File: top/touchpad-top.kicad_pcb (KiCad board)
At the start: 4 copper layers, 28.3 x 40 mm, 18 parts, among them P1 CONN_10, P2 CONN_5, U1 IQS572, U4 ESD

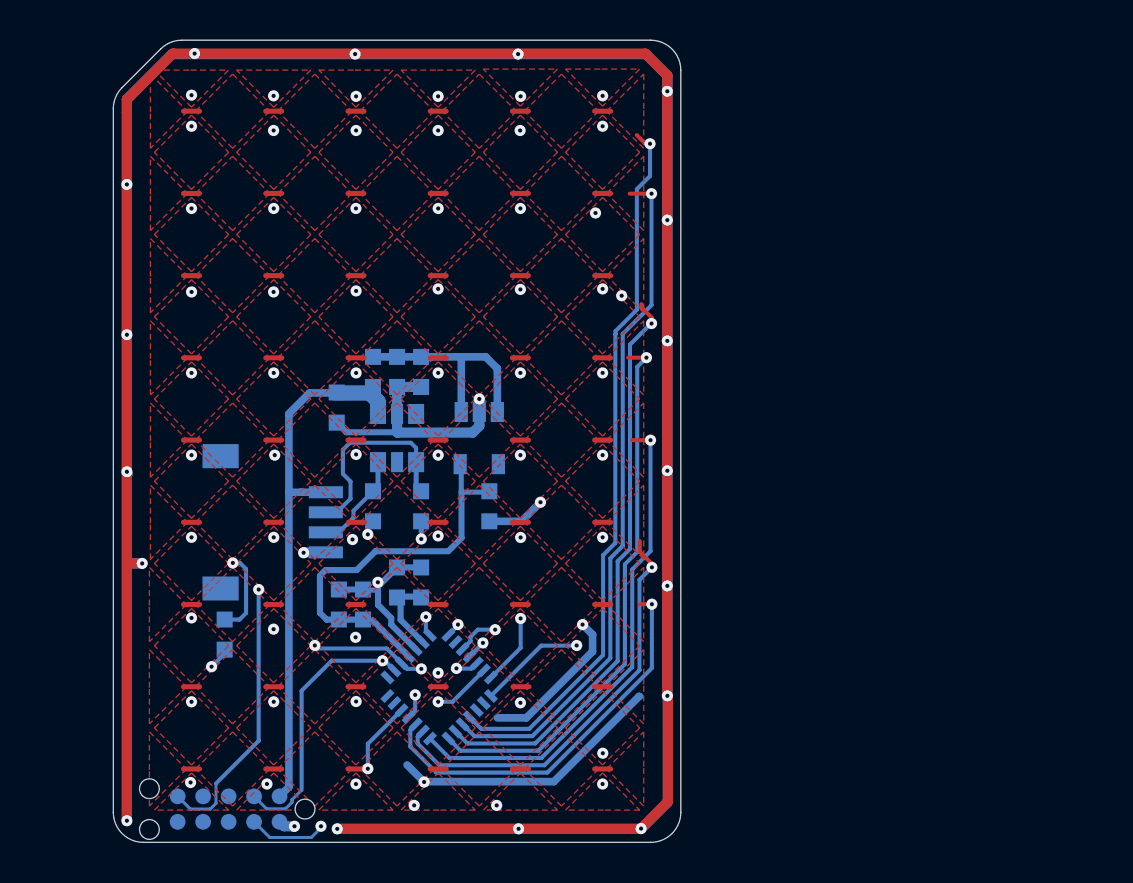
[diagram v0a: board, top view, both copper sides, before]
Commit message: Add GND island into capacitive pads.
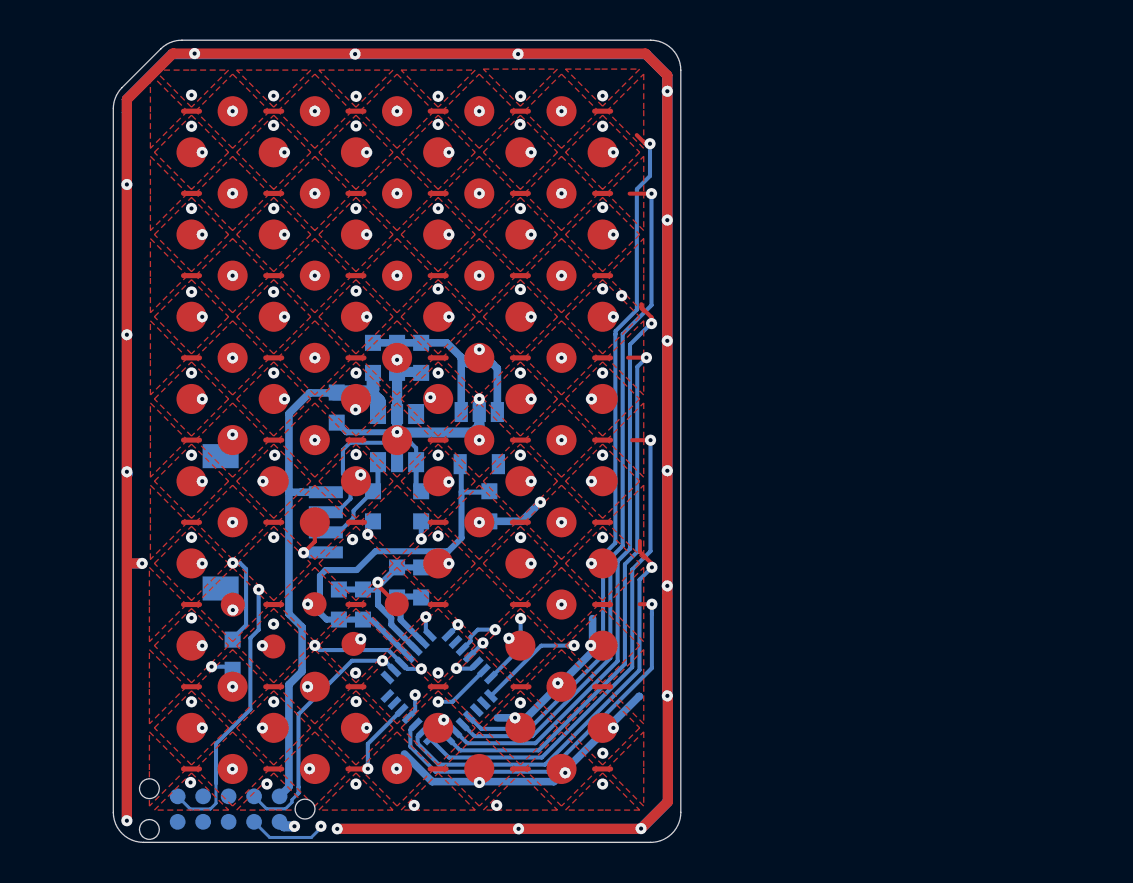
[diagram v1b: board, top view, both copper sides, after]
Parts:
- added hole: 1.5mm, UGL:smd_pad_1.5mm, F.Cu at (209.8, 154.8)
- added hole: 1.5mm, UGL:smd_pad_1.5mm, F.Cu at (211.8, 148.7)
- added hole: 1.5mm, UGL:smd_pad_1.5mm, F.Cu at (195.4, 148.7)
- added hole: 1.5mm, UGL:smd_pad_1.5mm, F.Cu at (215.9, 144.6)
- added hole: 1.5mm, UGL:smd_pad_1.5mm, F.Cu at (211.8, 144.6)
- added hole: 1.5mm, UGL:smd_pad_1.5mm, F.Cu at (207.8, 144.6)
- added hole: 1.5mm, UGL:smd_pad_1.5mm, F.Cu at (195.4, 144.6)
- added hole: 1.5mm, UGL:smd_pad_1.5mm, F.Cu at (215.9, 140.4)
- added hole: 1.5mm, UGL:smd_pad_1.5mm, F.Cu at (211.8, 140.4)
- added hole: 1.5mm, UGL:smd_pad_1.5mm, F.Cu at (207.8, 140.4)
- added hole: 1.5mm, UGL:smd_pad_1.5mm, F.Cu at (203.7, 140.4)
- added hole: 1.5mm, UGL:smd_pad_1.5mm, F.Cu at (197.5, 142.5)
- added hole: 1.5mm, UGL:smd_pad_1.5mm, F.Cu at (199.6, 140.4)
- added hole: 1.5mm, UGL:smd_pad_1.5mm, F.Cu at (195.4, 140.4)
- added hole: 1.5mm, UGL:smd_pad_1.5mm, F.Cu at (215.9, 136.3)
- added hole: 1.5mm, UGL:smd_pad_1.5mm, F.Cu at (211.8, 136.3)
- added hole: 1.5mm, UGL:smd_pad_1.5mm, F.Cu at (207.8, 136.3)
- added hole: 1.5mm, UGL:smd_pad_1.5mm, F.Cu at (203.7, 136.3)
- added hole: 1.5mm, UGL:smd_pad_1.5mm, F.Cu at (199.6, 136.3)
- added hole: 1.5mm, UGL:smd_pad_1.5mm, F.Cu at (195.4, 136.3)
- added hole: 1.5mm, UGL:smd_pad_1.5mm, F.Cu at (215.9, 132.2)
- added hole: 1.5mm, UGL:smd_pad_1.5mm, F.Cu at (211.8, 132.2)
- added hole: 1.5mm, UGL:smd_pad_1.5mm, F.Cu at (215.9, 152.8)
- added hole: 1.5mm, UGL:smd_pad_1.5mm, F.Cu at (207.8, 132.2)
- added hole: 1.5mm, UGL:smd_pad_1.5mm, F.Cu at (203.7, 132.2)
- added hole: 1.5mm, UGL:smd_pad_1.5mm, F.Cu at (199.6, 132.2)
- added hole: 1.5mm, UGL:smd_pad_1.5mm, F.Cu at (195.4, 132.2)
- added hole: 1.5mm, UGL:smd_pad_1.5mm, F.Cu at (215.9, 128.2)
- added hole: 1.5mm, UGL:smd_pad_1.5mm, F.Cu at (211.8, 128.2)
- added hole: 1.5mm, UGL:smd_pad_1.5mm, F.Cu at (207.8, 128.2)
- added hole: 1.5mm, UGL:smd_pad_1.5mm, F.Cu at (203.7, 128.2)
- added hole: 1.5mm, UGL:smd_pad_1.5mm, F.Cu at (199.6, 128.2)
- added hole: 1.5mm, UGL:smd_pad_1.5mm, F.Cu at (195.4, 128.2)
- added hole: 1.5mm, UGL:smd_pad_1.5mm, F.Cu at (211.8, 152.8)
- added hole: 1.5mm, UGL:smd_pad_1.5mm, F.Cu at (215.9, 124.0)
- added hole: 1.5mm, UGL:smd_pad_1.5mm, F.Cu at (211.8, 124.0)
- added hole: 1.5mm, UGL:smd_pad_1.5mm, F.Cu at (207.8, 124.0)
- added hole: 1.5mm, UGL:smd_pad_1.5mm, F.Cu at (203.7, 124.0)
- added hole: 1.5mm, UGL:smd_pad_1.5mm, F.Cu at (199.6, 124.0)
- added hole: 1.5mm, UGL:smd_pad_1.5mm, F.Cu at (195.4, 124.0)
- added hole: 1.5mm, UGL:smd_pad_1.5mm, F.Cu at (213.9, 154.8)
- added hole: 1.5mm, UGL:smd_pad_1.5mm, F.Cu at (205.7, 154.8)
- added hole: 1.5mm, UGL:smd_pad_1.5mm, F.Cu at (201.6, 154.8)
- added hole: 1.5mm, UGL:smd_pad_1.5mm, F.Cu at (197.5, 154.8)
- added hole: 1.5mm, UGL:smd_pad_1.5mm, F.Cu at (207.8, 152.8)
- added hole: 1.5mm, UGL:smd_pad_1.5mm, F.Cu at (213.9, 150.7)
- added hole: 1.5mm, UGL:smd_pad_1.5mm, F.Cu at (201.6, 150.7)
- added hole: 1.5mm, UGL:smd_pad_1.5mm, F.Cu at (197.5, 150.7)
- added hole: 1.5mm, UGL:smd_pad_1.5mm, F.Cu at (213.9, 146.6)
- added hole: 1.5mm, UGL:smd_pad_1.5mm, F.Cu at (213.9, 142.5)
- added hole: 1.5mm, UGL:smd_pad_1.5mm, F.Cu at (209.8, 142.5)
- added hole: 1.5mm, UGL:smd_pad_1.5mm, F.Cu at (201.6, 142.5)
- added hole: 1.5mm, UGL:smd_pad_1.5mm, F.Cu at (213.9, 138.4)
- added hole: 1.5mm, UGL:smd_pad_1.5mm, F.Cu at (209.8, 138.4)
- added hole: 1.5mm, UGL:smd_pad_1.5mm, F.Cu at (205.7, 138.4)
- added hole: 1.5mm, UGL:smd_pad_1.5mm, F.Cu at (203.7, 152.8)
- added hole: 1.5mm, UGL:smd_pad_1.5mm, F.Cu at (201.6, 138.4)
- added hole: 1.5mm, UGL:smd_pad_1.5mm, F.Cu at (197.5, 138.4)
- added hole: 1.5mm, UGL:smd_pad_1.5mm, F.Cu at (213.9, 134.3)
- added hole: 1.5mm, UGL:smd_pad_1.5mm, F.Cu at (209.8, 134.3)
- added hole: 1.5mm, UGL:smd_pad_1.5mm, F.Cu at (205.7, 134.3)
- added hole: 1.5mm, UGL:smd_pad_1.5mm, F.Cu at (201.6, 134.3)
- added hole: 1.5mm, UGL:smd_pad_1.5mm, F.Cu at (197.5, 134.3)
- added hole: 1.5mm, UGL:smd_pad_1.5mm, F.Cu at (213.9, 130.2)
- added hole: 1.5mm, UGL:smd_pad_1.5mm, F.Cu at (209.8, 130.2)
- added hole: 1.5mm, UGL:smd_pad_1.5mm, F.Cu at (205.7, 130.2)
- added hole: 1.5mm, UGL:smd_pad_1.5mm, F.Cu at (199.6, 152.8)
- added hole: 1.5mm, UGL:smd_pad_1.5mm, F.Cu at (201.6, 130.2)
- added hole: 1.5mm, UGL:smd_pad_1.5mm, F.Cu at (197.5, 130.2)
- added hole: 1.5mm, UGL:smd_pad_1.5mm, F.Cu at (213.9, 126.1)
- added hole: 1.5mm, UGL:smd_pad_1.5mm, F.Cu at (209.8, 126.1)
- added hole: 1.5mm, UGL:smd_pad_1.5mm, F.Cu at (205.7, 126.1)
- added hole: 1.5mm, UGL:smd_pad_1.5mm, F.Cu at (201.6, 126.1)
- added hole: 1.5mm, UGL:smd_pad_1.5mm, F.Cu at (197.5, 126.1)
- added hole: 1.5mm, UGL:smd_pad_1.5mm, F.Cu at (213.9, 122.0)
- added hole: 1.5mm, UGL:smd_pad_1.5mm, F.Cu at (209.8, 122.0)
- added hole: 1.5mm, UGL:smd_pad_1.5mm, F.Cu at (205.7, 122.0)
- added hole: 1.5mm, UGL:smd_pad_1.5mm, F.Cu at (195.4, 152.8)
- added hole: 1.5mm, UGL:smd_pad_1.5mm, F.Cu at (201.6, 122.0)
- added hole: 1.5mm, UGL:smd_pad_1.5mm, F.Cu at (197.5, 122.0)
- added hole: 1.5mm, UGL:smd_pad_1.5mm, F.Cu at (215.9, 148.7)
- added pad: 1.2mm, UGL:smd_pad_1.2mm, F.Cu at (203.5, 148.6)
- added pad: 1.2mm, UGL:smd_pad_1.2mm, F.Cu at (197.5, 146.6)
- added pad: 1.2mm, UGL:smd_pad_1.2mm, F.Cu at (199.5, 148.7)
- added pad: 1.2mm, UGL:smd_pad_1.2mm, F.Cu at (205.7, 146.6)
- added pad: 1.2mm, UGL:smd_pad_1.2mm, F.Cu at (201.6, 146.6)
- moved C1 1.08 mm to (197.5, 149.1)
- moved C2 0.70 mm to (205.7, 134.3)
- moved C8 0.70 mm to (206.9, 134.3)
- moved FB2 0.70 mm to (204.5, 134.3)
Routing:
- net GND: track 471.4 -> 476.0 mm, vias 26 -> 108
- net /VCC_BOTTOM: track 26.8 -> 28.4 mm
- net /RX2: track 41.5 -> 42.6 mm
- net /SDA: track 21.1 -> 20.4 mm
- net /RX3: track 39.1 -> 39.7 mm

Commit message: Bump top board version to 2.3.0
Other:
- board text added: "PCB_ID: touchpad_top_2.3.0"
- board text removed: "PCB_ID: touchpad_top_2.2.0"

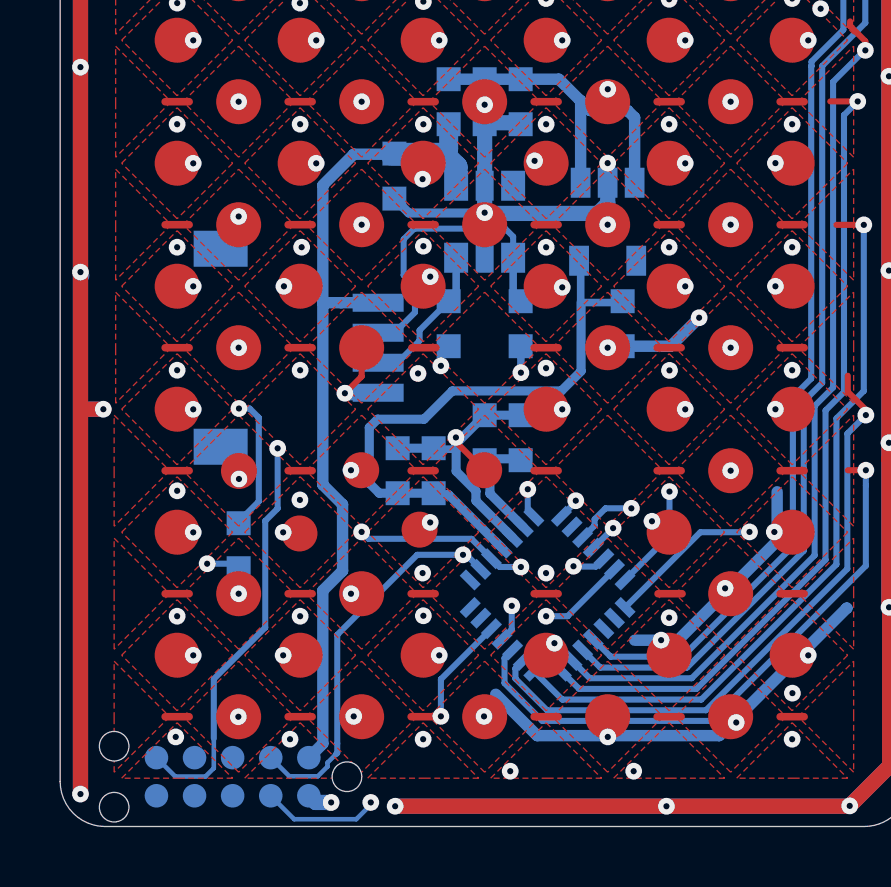
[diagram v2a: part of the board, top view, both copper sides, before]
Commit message: Modified SCL and SDA routing.
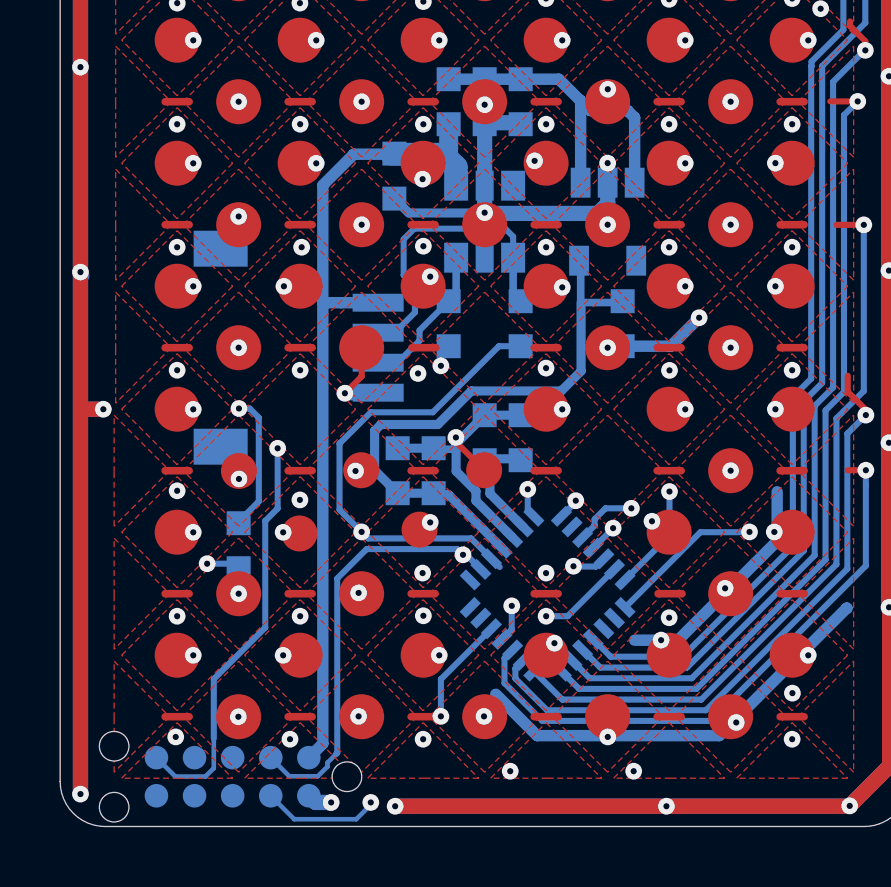
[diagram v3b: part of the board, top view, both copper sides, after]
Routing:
- net /SCL: track 26.6 -> 29.4 mm, vias 4 -> 2
- net /SDA: track 20.4 -> 21.7 mm
- net +3V3: track 19.4 -> 18.8 mm
- net /VCC_BOTTOM: track 28.4 -> 27.9 mm

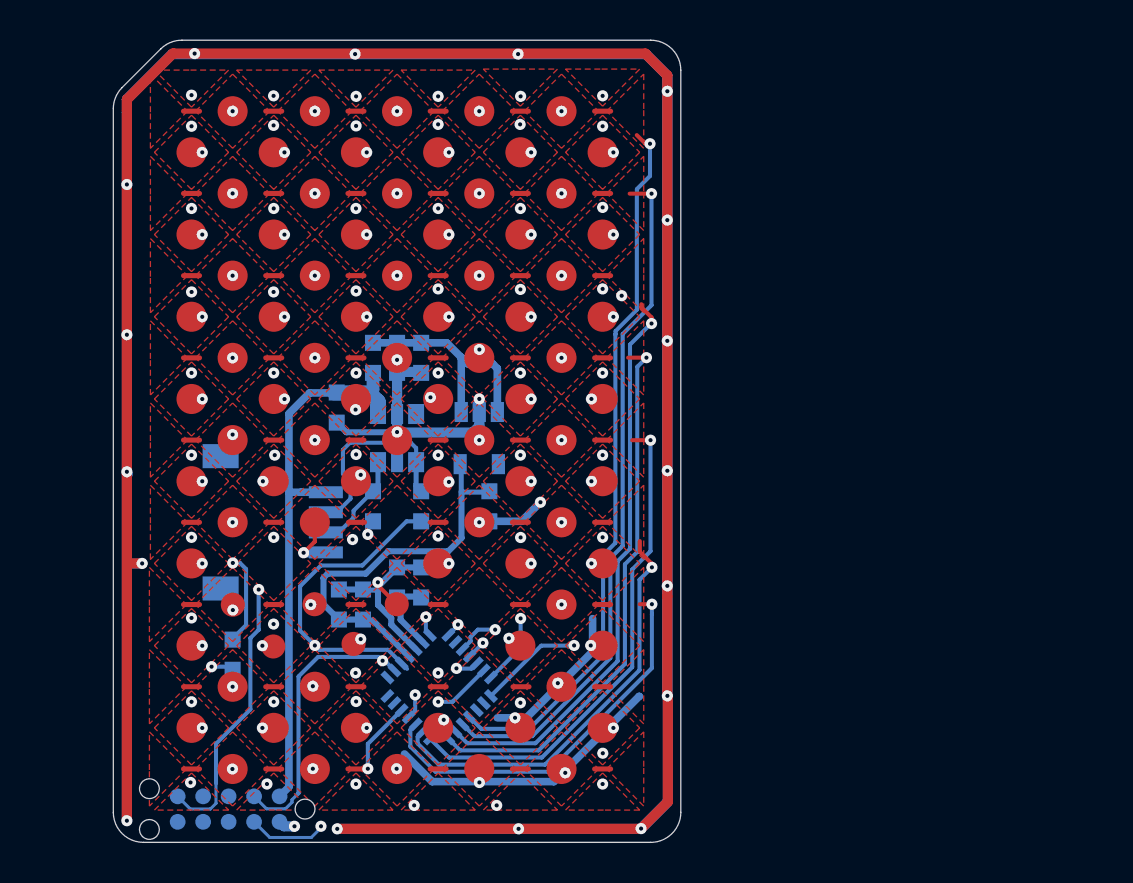
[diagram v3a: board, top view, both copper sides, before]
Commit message: Change board stackup and remove gnd islands.
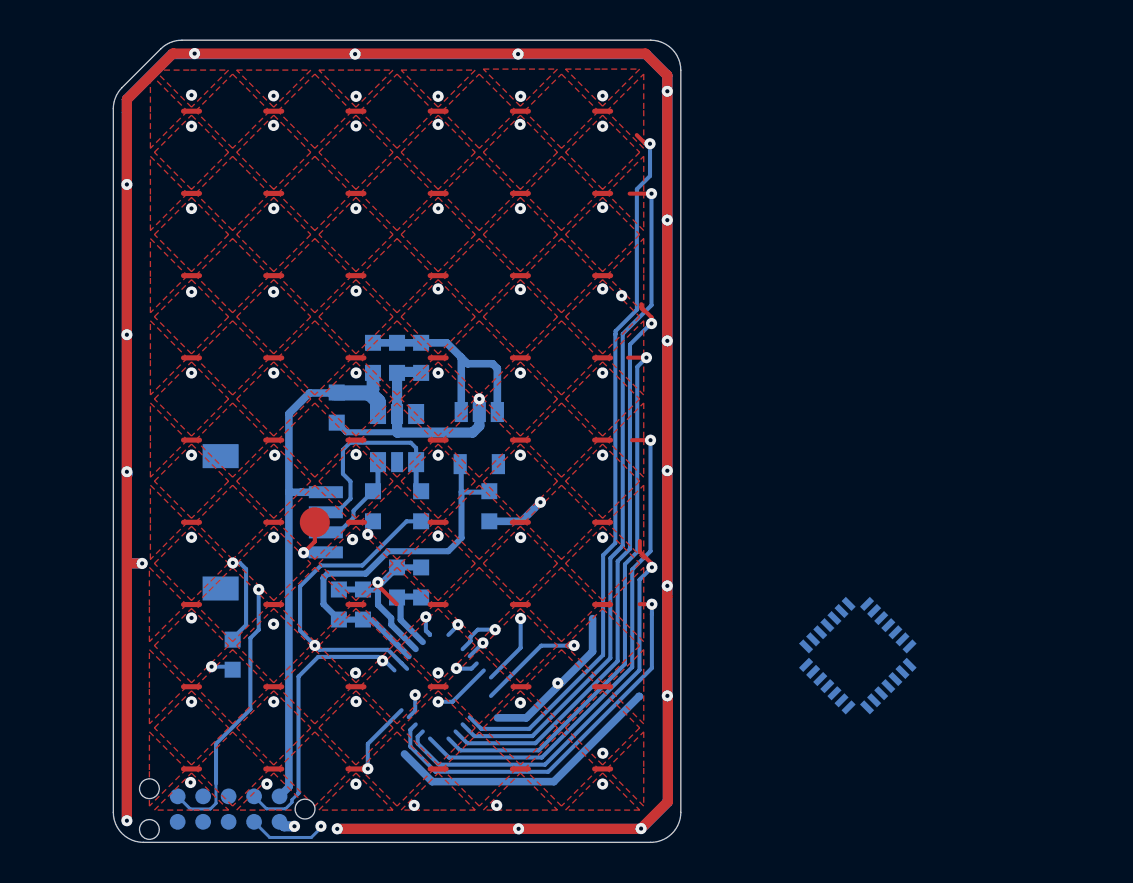
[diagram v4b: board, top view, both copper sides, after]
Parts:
- removed the hole at (209.8, 154.8)
- removed the hole at (211.8, 148.7)
- removed the hole at (195.4, 148.7)
- removed the hole at (215.9, 144.6)
- removed the hole at (211.8, 144.6)
- removed the hole at (207.8, 144.6)
- removed the hole at (195.4, 144.6)
- removed the hole at (215.9, 140.4)
- removed the hole at (211.8, 140.4)
- removed the hole at (207.8, 140.4)
- removed the hole at (203.7, 140.4)
- removed the hole at (197.5, 142.5)
- removed the hole at (199.6, 140.4)
- removed the hole at (195.4, 140.4)
- removed the hole at (215.9, 136.3)
- removed the hole at (211.8, 136.3)
- removed the hole at (207.8, 136.3)
- removed the hole at (203.7, 136.3)
- removed the hole at (199.6, 136.3)
- removed the hole at (195.4, 136.3)
- removed the hole at (215.9, 132.2)
- removed the hole at (211.8, 132.2)
- removed the hole at (215.9, 152.8)
- removed the hole at (207.8, 132.2)
- removed the hole at (203.7, 132.2)
- removed the hole at (199.6, 132.2)
- removed the hole at (195.4, 132.2)
- removed the hole at (215.9, 128.2)
- removed the hole at (211.8, 128.2)
- removed the hole at (207.8, 128.2)
- removed the hole at (203.7, 128.2)
- removed the hole at (199.6, 128.2)
- removed the hole at (195.4, 128.2)
- removed the hole at (211.8, 152.8)
- removed the hole at (215.9, 124.0)
- removed the hole at (211.8, 124.0)
- removed the hole at (207.8, 124.0)
- removed the hole at (203.7, 124.0)
- removed the hole at (199.6, 124.0)
- removed the hole at (195.4, 124.0)
- removed the hole at (213.9, 154.8)
- removed the hole at (205.7, 154.8)
- removed the hole at (201.6, 154.8)
- removed the hole at (197.5, 154.8)
- removed the hole at (207.8, 152.8)
- removed the hole at (213.9, 150.7)
- removed the hole at (201.6, 150.7)
- removed the hole at (197.5, 150.7)
- removed the hole at (213.9, 146.6)
- removed the hole at (213.9, 142.5)
- removed the hole at (209.8, 142.5)
- removed the hole at (213.9, 138.4)
- removed the hole at (209.8, 138.4)
- removed the hole at (205.7, 138.4)
- removed the hole at (203.7, 152.8)
- removed the hole at (201.6, 138.4)
- removed the hole at (197.5, 138.4)
- removed the hole at (213.9, 134.3)
- removed the hole at (209.8, 134.3)
- removed the hole at (205.7, 134.3)
- removed the hole at (201.6, 134.3)
- removed the hole at (197.5, 134.3)
- removed the hole at (213.9, 130.2)
- removed the hole at (209.8, 130.2)
- removed the hole at (205.7, 130.2)
- removed the hole at (199.6, 152.8)
- removed the hole at (201.6, 130.2)
- removed the hole at (197.5, 130.2)
- removed the hole at (213.9, 126.1)
- removed the hole at (209.8, 126.1)
- removed the hole at (205.7, 126.1)
- removed the hole at (201.6, 126.1)
- removed the hole at (197.5, 126.1)
- removed the hole at (213.9, 122.0)
- removed the hole at (209.8, 122.0)
- removed the hole at (205.7, 122.0)
- removed the hole at (195.4, 152.8)
- removed the hole at (201.6, 122.0)
- removed the hole at (197.5, 122.0)
- removed the hole at (215.9, 148.7)
- removed pad (x5): 1.2mm, UGL:smd_pad_1.2mm
- moved U1 20.9 mm to (228.7, 149.1)
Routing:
- net GND: track 476.0 -> 290.3 mm, vias 108 -> 25
- net /RX0: track 53.0 -> 2.15 mm
- net /RX1: track 46.4 -> 0.94 mm
- net /RX2: track 42.6 -> 1.13 mm
- net /RX3: track 39.7 -> 2.92 mm
- net /RX4: track 39.8 -> 3.56 mm
- net /RX5: track 41.4 -> 5.30 mm
- net /RDY: track 25.3 -> 14.5 mm
- net /NRST: track 16.5 -> 5.79 mm
- net /SCL: track 29.4 -> 19.7 mm
- net /SDA: track 21.7 -> 15.0 mm
- removed copper zone on In2.Cu, net GND
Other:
- copper layers 4 -> 2
